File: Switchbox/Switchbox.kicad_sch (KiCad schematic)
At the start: 25 parts, among them J1 USB-C_connector, SW1 SW_SPDT, SW2 SW_SPDT, SW3 SW_SPDT, SW4 SW_SPDT, SW5 SW_Push, U1 TPS63031DSKT

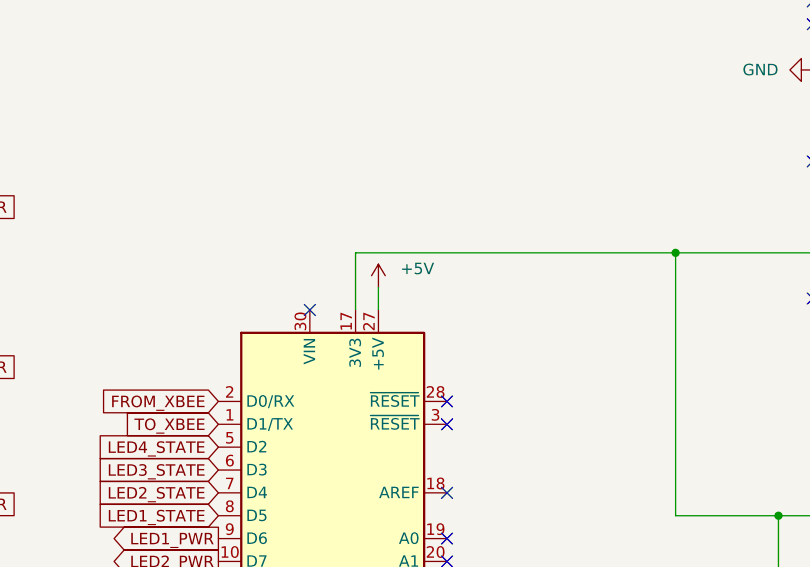
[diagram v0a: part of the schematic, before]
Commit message: added known footprints
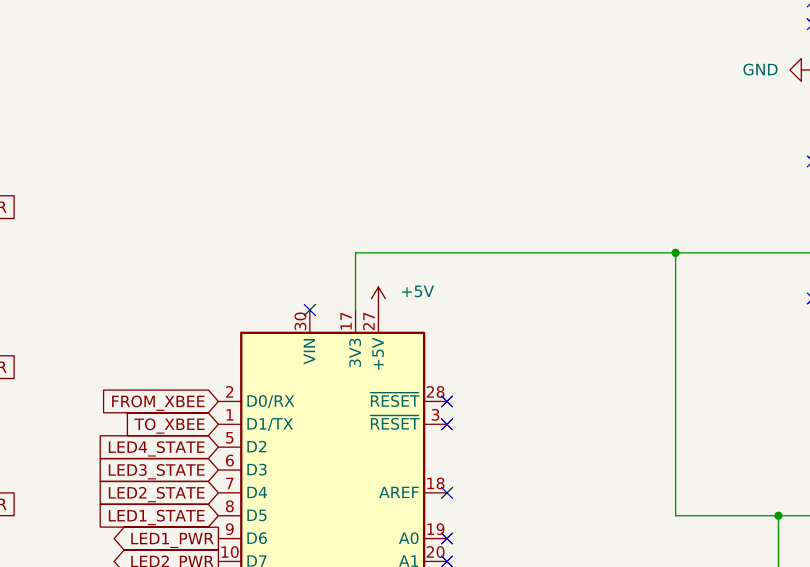
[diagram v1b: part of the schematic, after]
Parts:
- D1, D2, D3, D4, D5, D6: footprint (none) -> LED_THT:LED_D5.0mm
- J1: footprint CONN_10164359-00011LF_AMP -> switchbox_footprints:CONN_10164359-00011LF_AMP
- R1, R2, R3, R4, R5, R6, R7: footprint (none) -> Resistor_THT:R_Axial_DIN0207_L6.3mm_D2.5mm_P7.62mm_Horizontal
- U1: footprint DSK0010A -> switchbox_footprints:DSK0010A
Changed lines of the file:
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@@
 	(wire
 		(pts
-			(xy 119.38 63.5) (xy 119.38 66.04)
-		)
-		(stroke
-			(width 0)
-			(type default)
-		)
-	)
-	(wire
-		(pts
 			(xy 116.84 59.69) (xy 116.84 66.04)
 		)
@@
 	(symbol
 		(lib_id "power:+5V")
-		(at 119.38 63.5 0)
+		(at 119.38 66.04 0)
 		(unit 1)
 		(exclude_from_sim no)
@@
 		(dnp no)
 		(property "Reference" "#PWR0102"
-			(at 119.38 67.31 0)
+			(at 119.38 69.85 0)
 			(effects
 				(font
@@
 		)
 		(property "Value" "+5V"
-			(at 123.698 61.468 0)
+			(at 123.698 64.008 0)
 			(effects
 				(font
@@
 		)
 		(property "Footprint" ""
-			(at 119.38 63.5 0)
+			(at 119.38 66.04 0)
 			(effects
 				(font
@@
 		)
 		(property "Datasheet" ""
-			(at 119.38 63.5 0)
+			(at 119.38 66.04 0)
 			(effects
 				(font
@@
 		)
 		(property "Description" "Power symbol creates a global label with name \"+5V\""
-			(at 119.38 63.5 0)
+			(at 119.38 66.04 0)
 			(effects
 				(font
@@
 			)
 		)
-		(property "Footprint" ""
+		(property "Footprint" "Resistor_THT:R_Axial_DIN0207_L6.3mm_D2.5mm_P7.62mm_Horizontal"
 			(at 59.69 74.168 90)
 			(effects
@@
 			)
 		)
-		(property "Footprint" "CONN_10164359-00011LF_AMP"
+		(property "Footprint" "switchbox_footprints:CONN_10164359-00011LF_AMP"
 			(at 217.17 33.02 0)
 			(effects
@@
 			)
 		)
-		(property "Footprint" ""
+		(property "Footprint" "LED_THT:LED_D5.0mm"
 			(at 53.34 125.73 0)
 			(effects
@@
 			)
 		)
-		(property "Footprint" ""
+		(property "Footprint" "Resistor_THT:R_Axial_DIN0207_L6.3mm_D2.5mm_P7.62mm_Horizontal"
 			(at 59.69 127.508 90)
 			(effects
@@
 			)
 		)
-		(property "Footprint" ""
+		(property "Footprint" "LED_THT:LED_D5.0mm"
 			(at 53.34 102.87 0)
 			(effects
@@
 			)
 		)
-		(property "Footprint" ""
+		(property "Footprint" "Resistor_THT:R_Axial_DIN0207_L6.3mm_D2.5mm_P7.62mm_Horizontal"
 			(at 59.69 104.648 90)
 			(effects
@@
 			)
 		)
-		(property "Footprint" ""
+		(property "Footprint" "Resistor_THT:R_Axial_DIN0207_L6.3mm_D2.5mm_P7.62mm_Horizontal"
 			(at 59.69 89.408 90)
 			(effects
@@
 			)
 		)
-		(property "Footprint" ""
+		(property "Footprint" "Resistor_THT:R_Axial_DIN0207_L6.3mm_D2.5mm_P7.62mm_Horizontal"
 			(at 59.69 116.078 90)
 			(effects
@@
 			)
 		)
-		(property "Footprint" ""
+		(property "Footprint" "Resistor_THT:R_Axial_DIN0207_L6.3mm_D2.5mm_P7.62mm_Horizontal"
 			(at 59.69 56.388 90)
 			(effects
@@
 			)
 		)
-		(property "Footprint" ""
+		(property "Footprint" "Resistor_THT:R_Axial_DIN0207_L6.3mm_D2.5mm_P7.62mm_Horizontal"
 			(at 87.122 129.54 90)
 			(effects
@@
 			)
 		)
-		(property "Footprint" ""
+		(property "Footprint" "LED_THT:LED_D5.0mm"
 			(at 53.34 87.63 0)
 			(effects
@@
 			)
 		)
-		(property "Footprint" ""
+		(property "Footprint" "LED_THT:LED_D5.0mm"
 			(at 53.34 72.39 0)
 			(effects
@@
 			)
 		)
-		(property "Footprint" "DSK0010A"
+		(property "Footprint" "switchbox_footprints:DSK0010A"
 			(at 185.42 49.53 0)
 			(effects
@@
 			)
 		)
-		(property "Footprint" ""
+		(property "Footprint" "LED_THT:LED_D5.0mm"
 			(at 53.34 54.61 0)
 			(effects
@@
 			)
 		)
-		(property "Footprint" ""
+		(property "Footprint" "LED_THT:LED_D5.0mm"
 			(at 53.34 114.3 0)
 			(effects

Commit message: stole buck converter
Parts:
- removed U1: TPS63031DSKT, switchbox_footprints:DSK0010A, symbol killswitch:TPS63031DSKT
- added C2: 0.1µF, symbol Device:C
- added C2: 10µF, symbol Device:C
- added C3, C4: 22µF, symbol Device:C
- added L1: 4.7µH, symbol Device:L
- added R3a1, R3b1: 100k, symbol Device:R
- added U2: AP63203WU, Package_TO_SOT_SMD:TSOT-23-6, symbol Regulator_Switching:AP63203WU
- C1: value 100n -> 100nF
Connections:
- net GND: now also C2.2, C3.2, C4.2, R3b1.2, U2.4 (GND)
- net 3.3VBuck: now reaches A2.17 (3V3), C5.1, C7.1, XBEE1.1 (VCC)
- net 3.3VBuck: now also C3.1, C4.1, L1.2, U2.1 (FB)
- net Sys_Vin: now reaches J1.B5 (VBUS)
- net Sys_Vin: now also C2.1, R3a1.2, U2.3 (IN)
- new net: C2.2, L1.1, U2.5 (SW)
- new net: R3a1.1, R3b1.1, U2.2 (EN)
- new net: C2.1, U2.6 (BST)
- no-connect marks 41 -> 33
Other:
- moved on the sheet: J1

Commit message: added on/off for switchbox
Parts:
- added SW6: SW_Push_SPDT, symbol Switch:SW_Push_SPDT
- R3a1, R3b1: footprint (none) -> Resistor_THT:R_Axial_DIN0207_L6.3mm_D2.5mm_P7.62mm_Horizontal
- renumbered C2 to C1, C7 to C6, C1 to C7
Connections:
- net 3.3VBuck: now also SW6.3 (C); no longer A2.17 (3V3), C5.1, C6.1, XBEE1.1 (VCC)
- net GND: now also SW6.1 (A)
- new net BOX_STATE: A2.17 (3V3), C5.1, C6.1, SW6.2 (B), XBEE1.1 (VCC)
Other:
- moved on the sheet: C1, C2, C3, C4, J1, L1, R3a1, R3b1, U2

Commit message: basic switch footprint
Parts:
- C7: footprint (none) -> Capacitor_SMD:CP_Elec_3x5.3
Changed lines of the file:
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@@
 			)
 		)
-		(property "Footprint" ""
+		(property "Footprint" "Capacitor_SMD:CP_Elec_3x5.3"
 			(at 70.8152 147.32 0)
 			(effects

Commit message: added xbee footprint
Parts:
- XBEE1: footprint ElectronicsFootprints:XBee -> switchbox_footprints:xbee
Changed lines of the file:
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@@
 			)
 		)
-		(property "Footprint" "ElectronicsFootprints:XBee"
+		(property "Footprint" "switchbox_footprints:xbee"
 			(at 228.6 91.44 0)
 			(effects

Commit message: reassigned some footprints
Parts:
- C1, C2, C3, C4: footprint (none) -> Capacitor_SMD:C_0201_0603Metric_Pad0.64x0.40mm_HandSolder
- L1: footprint (none) -> Inductor_SMD:L_0201_0603Metric_Pad0.64x0.40mm_HandSolder
- SW1, SW2, SW3, SW4: footprint (none) -> switchbox_footprints:SW_SPDT
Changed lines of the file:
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@@
 			)
 		)
-		(property "Footprint" ""
+		(property "Footprint" "Inductor_SMD:L_0201_0603Metric_Pad0.64x0.40mm_HandSolder"
 			(at 163.83 25.4 0)
 			(effects
@@
 			)
 		)
-		(property "Footprint" ""
+		(property "Footprint" "Capacitor_SMD:C_0201_0603Metric_Pad0.64x0.40mm_HandSolder"
 			(at 182.5752 38.1 0)
 			(effects
@@
 			)
 		)
-		(property "Footprint" ""
+		(property "Footprint" "switchbox_footprints:SW_SPDT"
 			(at 34.29 69.85 0)
 			(effects
@@
 			)
 		)
-		(property "Footprint" ""
+		(property "Footprint" "switchbox_footprints:SW_SPDT"
 			(at 34.29 100.33 0)
 			(effects
@@
 			)
 		)
-		(property "Footprint" ""
+		(property "Footprint" "switchbox_footprints:SW_SPDT"
 			(at 34.29 85.09 0)
 			(effects
@@
 			)
 		)
-		(property "Footprint" ""
+		(property "Footprint" "Capacitor_SMD:C_0201_0603Metric_Pad0.64x0.40mm_HandSolder"
 			(at 158.75 26.9748 0)
 			(effects
@@
 			)
 		)
-		(property "Footprint" ""
+		(property "Footprint" "Capacitor_SMD:C_0201_0603Metric_Pad0.64x0.40mm_HandSolder"
 			(at 115.2652 33.02 0)
 			(effects
@@
 			)
 		)
-		(property "Footprint" ""
+		(property "Footprint" "switchbox_footprints:SW_SPDT"
 			(at 34.29 52.07 0)
 			(effects
@@
 			)
 		)
-		(property "Footprint" ""
+		(property "Footprint" "Capacitor_SMD:C_0201_0603Metric_Pad0.64x0.40mm_HandSolder"
 			(at 172.4152 38.1 0)
 			(effects

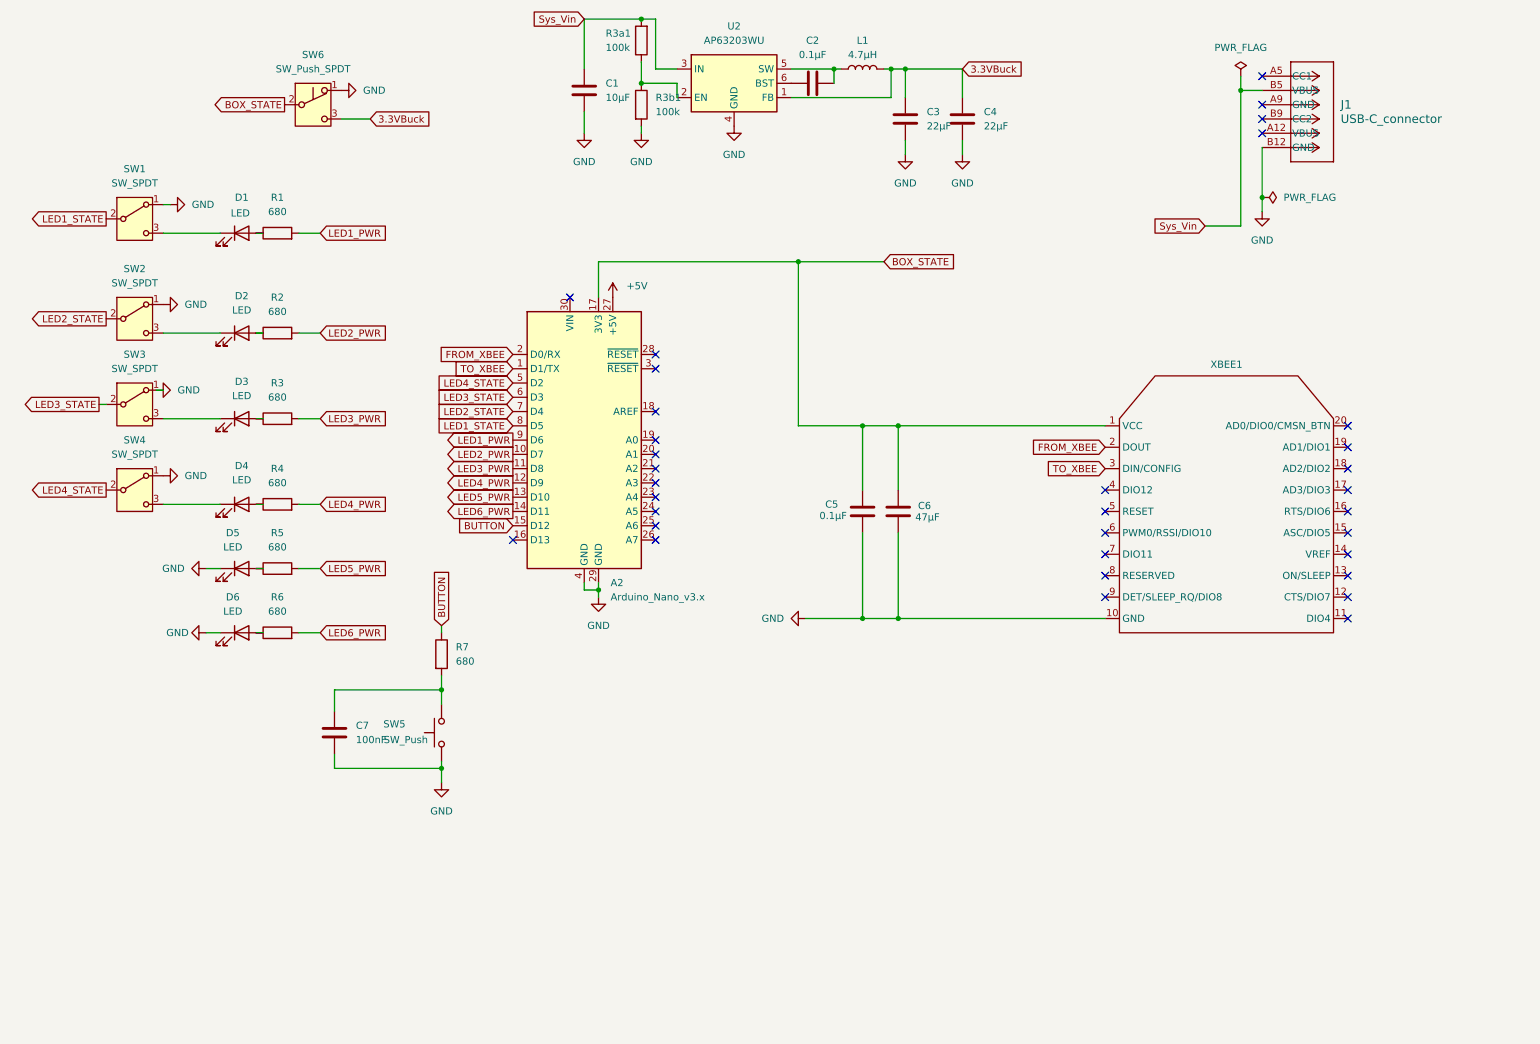
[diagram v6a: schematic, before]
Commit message: added button footprint
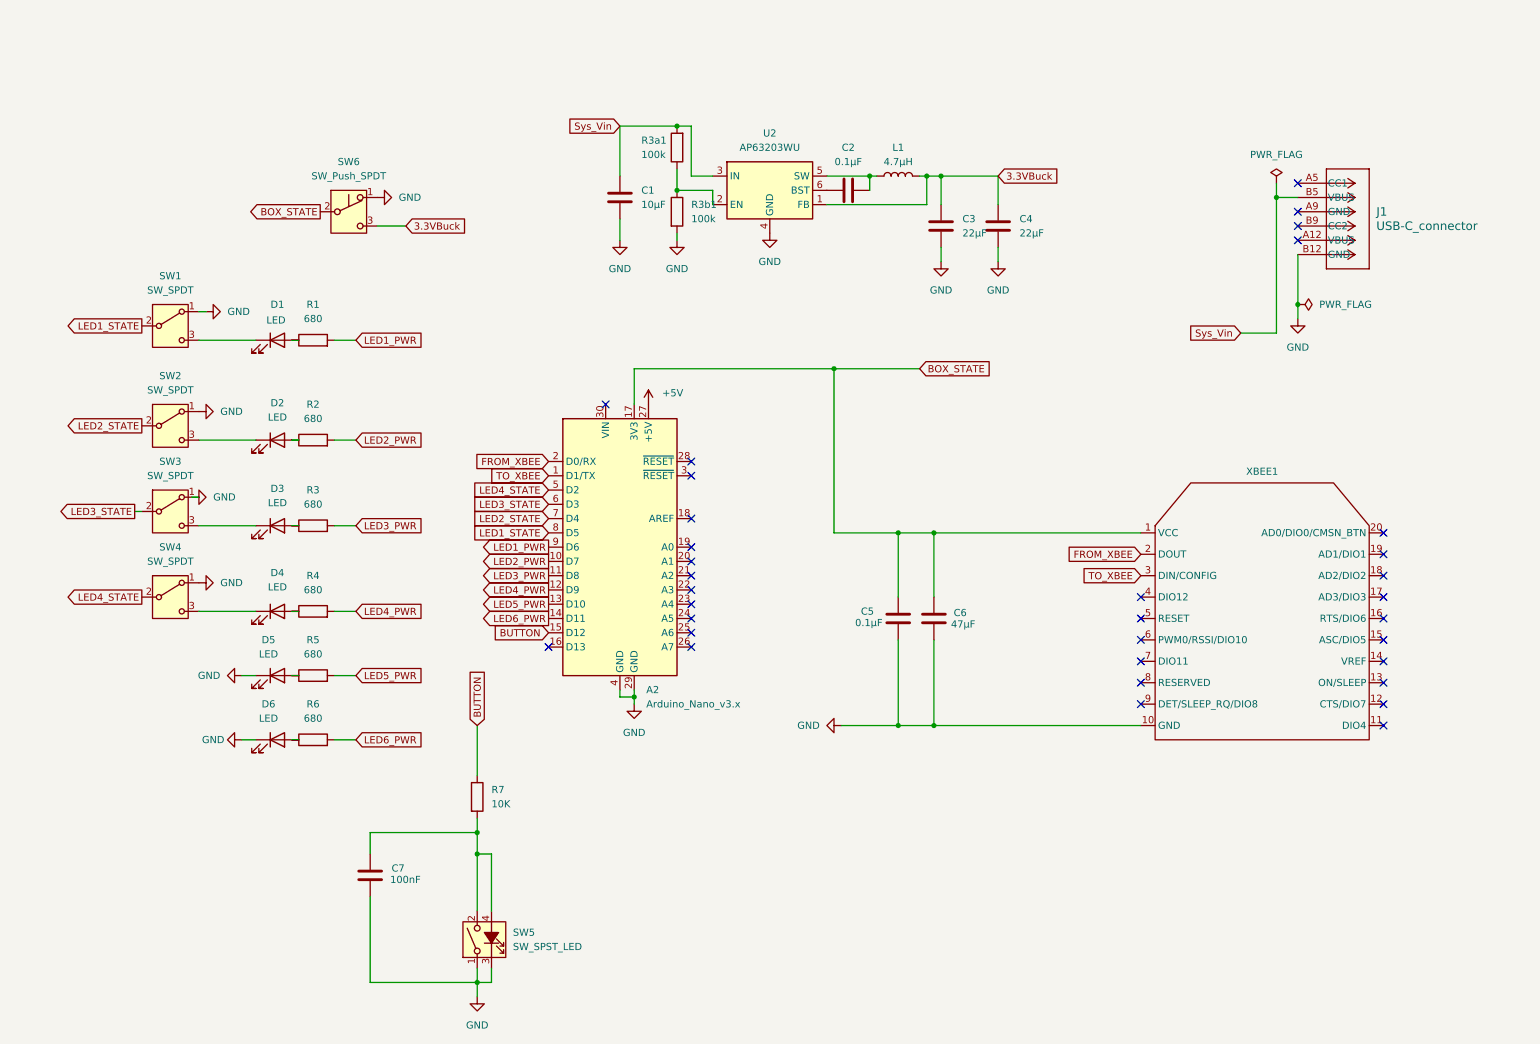
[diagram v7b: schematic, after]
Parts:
- removed SW5: SW_Push, symbol Switch:SW_Push
- added SW5: SW_SPST_LED, switchbox_footprints:SW_SPDT, symbol Switch:SW_SPST_LED
- C1, C2, C3, C4: footprint Capacitor_SMD:C_0201_0603Metric_Pad0.64x0.40mm_HandSolder -> (none)
- C7: footprint Capacitor_SMD:CP_Elec_3x5.3 -> (none)
- R7: value 680 -> 10K
- SW6: footprint (none) -> switchbox_footprints:SW_SPDT
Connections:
- net GND: now also SW5.1, SW5.3 (K)
- net at C7.1, R7.2: now also SW5.2, SW5.4 (A)
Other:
- moved on the sheet: A2, C1, C2, C3, C4, C5, C6, C7, D1, D2, D3, D4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

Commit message: forgot to assign oops
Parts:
- SW5: footprint switchbox_footprints:SW_SPDT -> switchbox_footprints:SPST_BUTTON_1190
- SW6: value SW_Push_SPDT -> SW_SPDT_BOX
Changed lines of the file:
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@@
 			)
 		)
-		(property "Value" "SW_Push_SPDT"
+		(property "Value" "SW_SPDT_BOX"
 			(at 72.39 44.45 0)
 			(effects
@@
 			)
 		)
-		(property "Footprint" "switchbox_footprints:SW_SPDT"
+		(property "Footprint" "switchbox_footprints:SPST_BUTTON_1190"
 			(at 90.17 180.34 0)
 			(effects
